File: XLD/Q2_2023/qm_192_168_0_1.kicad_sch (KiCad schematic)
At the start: 113 parts

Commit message: mend
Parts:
- renumbered MX701 to MX1, MX710 to MX10, MX711 to MX11, MX712 to MX12, MX713 to MX13, MX714 to MX14, MX715 to MX15, MX716 to MX16, MX717 to MX17, MX718 to MX18, MX719 to MX19, MX702 to MX2, MX720 to MX20, MX721 to MX21, MX722 to MX22, MX723 to MX23, MX724 to MX24, MX725 to MX25, MX726 to MX26, MX727 to MX27, MX728 to MX28, MX729 to MX29, MX703 to MX3, MX730 to MX30, MX731 to MX31, MX732 to MX32, MX733 to MX33, MX734 to MX34, MX735 to MX35, MX704 to MX4, MX705 to MX5, MX706 to MX6, MX707 to MX7, MX708 to MX8, MX709 to MX9
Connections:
- net ERA_01: now also LO5.
- net ERA_02: now also LO6.
- net ERA_03: now also LO2.
- net ERA_04: now also LO7.
- net ERA_05: now also LO3.
- net ERA_06: now also LO8.
- net ERA_07: now also LO4.
- net ERA_08: now also LO9.
- net LO_01: now also LO10.
- net LO_02: now also LO11.
- net LO_03: now also LO13.
- net LO_04: now also LO14.
- net LO_05: now also LO15.
- net LO_06: now also LO16.
- net LO_08: now also LO12.
- net at Splitter17.: now also Splitter18.; no longer Splitter16.
- net at Splitter18.: no longer Splitter17.
- net at Splitter6.: now also Splitter5.; no longer Splitter8.
- net at Splitter10.: now also Splitter9.; no longer Splitter8.
- net at Splitter22.: no longer Splitter21.
- net at Splitter20.: no longer Splitter21.
- net at Splitter7.: no longer Splitter6.
- net at Splitter5.: no longer Splitter6.
- net at Splitter14.: now also Splitter13.
- net at Splitter13.: now also Splitter12.; no longer Splitter14.
- net at Splitter11.: now also Splitter10.
- net at Splitter12.: no longer Splitter13.
- net at Splitter1.: no longer Splitter2.
- net at Splitter3.: no longer Splitter2.
- net at Splitter4.: now also Splitter3.
- new net: Splitter16., Splitter17.
- new net: Splitter15., Splitter17.
- new net: Splitter6., Splitter8.
- new net: Splitter10., Splitter8.
- new net: Splitter21., Splitter22.
- new net: Splitter20., Splitter21.
- new net: Splitter6., Splitter7.
- new net: Splitter13., Splitter15.
- new net: Splitter1., Splitter2.
- new net: Splitter2., Splitter3.
- now unconnected: Splitter3.
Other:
- moved on the sheet: BT1, BT10, BT11, BT12, BT13, BT14, BT15, BT16, BT2, BT3, BT4, BT5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

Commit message: more updates
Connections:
- net at Splitter17.: now also Splitter18.; no longer Splitter16.
- net at Splitter18.: no longer Splitter17.
- net at Splitter6.: now also Splitter5.; no longer Splitter8.
- net at Splitter10.: now also Splitter9.; no longer Splitter8.
- net at Splitter22.: no longer Splitter21.
- net at Splitter20.: no longer Splitter21.
- net at Splitter7.: no longer Splitter6.
- net at Splitter5.: no longer Splitter6.
- net at Splitter14.: now also Splitter13.
- net at Splitter13.: now also Splitter12.; no longer Splitter14.
- net at Splitter11.: now also Splitter10.
- net at Splitter12.: no longer Splitter13.
- net at Splitter1.: no longer Splitter2.
- net at Splitter3.: no longer Splitter2.
- net at Splitter4.: now also Splitter3.
- new net: Splitter16., Splitter17.
- new net: Splitter15., Splitter17.
- new net: Splitter6., Splitter8.
- new net: Splitter10., Splitter8.
- new net: Splitter21., Splitter22.
- new net: Splitter20., Splitter21.
- new net: Splitter6., Splitter7.
- new net: Splitter13., Splitter15.
- new net: Splitter1., Splitter2.
- new net: Splitter2., Splitter3.
- now unconnected: Splitter3.

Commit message: Improvements to library components, title, date
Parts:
- MX1, MX2, MX3: value SpinQ_IQ -> SpinQ; symbol Quantum Computing:SpinQ_IQ -> Quantum Computing:Mixer IQ SpinQ
- MX10, MX11, MX29, MX30, MX31: value Marki_IQ -> Marki; symbol Quantum Computing:Marki_IQ -> Quantum Computing:Mixer IQ Marki
- MX12: renamed from MX21; value SpinQ_IQ -> SpinQ; symbol Quantum Computing:SpinQ_IQ -> Quantum Computing:Mixer IQ SpinQ
- MX13: renamed from MX16; value Marki_IQ -> Marki; symbol Quantum Computing:Marki_IQ -> Quantum Computing:Mixer IQ Marki
- MX14: renamed from MX17; value Marki_IQ -> Marki; symbol Quantum Computing:Marki_IQ -> Quantum Computing:Mixer IQ Marki
- MX15: renamed from MX22; value SpinQ_IQ -> SpinQ; symbol Quantum Computing:SpinQ_IQ -> Quantum Computing:Mixer IQ SpinQ
- MX16: renamed from MX23; value Marki_IQ -> Marki; symbol Quantum Computing:Marki_IQ -> Quantum Computing:Mixer IQ Marki
- MX17: renamed from MX24; value Marki_IQ -> Marki; symbol Quantum Computing:Marki_IQ -> Quantum Computing:Mixer IQ Marki
- MX18: renamed from MX4; value SpinQ_IQ -> SpinQ; symbol Quantum Computing:SpinQ_IQ -> Quantum Computing:Mixer IQ SpinQ
- MX19: renamed from MX5; value SpinQ_IQ -> SpinQ; symbol Quantum Computing:SpinQ_IQ -> Quantum Computing:Mixer IQ SpinQ
- MX20: renamed from MX27; value Marki_IQ -> Marki; symbol Quantum Computing:Marki_IQ -> Quantum Computing:Mixer IQ Marki
- MX21: renamed from MX6; value SpinQ_IQ -> SpinQ; symbol Quantum Computing:SpinQ_IQ -> Quantum Computing:Mixer IQ SpinQ
- MX22: renamed from MX15; value SpinQ_IQ -> SpinQ; symbol Quantum Computing:SpinQ_IQ -> Quantum Computing:Mixer IQ SpinQ
- MX23: renamed from MX28; value Marki_IQ -> Marki; symbol Quantum Computing:Marki_IQ -> Quantum Computing:Mixer IQ Marki
- MX24: renamed from MX34; value Marki_IQ -> Marki; symbol Quantum Computing:Marki_IQ -> Quantum Computing:Mixer IQ Marki
- MX25: renamed from MX35; value Marki_IQ -> Marki; symbol Quantum Computing:Marki_IQ -> Quantum Computing:Mixer IQ Marki
- MX26: renamed from MX13; value Marki_IQ -> Marki; symbol Quantum Computing:Marki_IQ -> Quantum Computing:Mixer IQ Marki
- MX27: renamed from MX14; value Marki_IQ -> Marki; symbol Quantum Computing:Marki_IQ -> Quantum Computing:Mixer IQ Marki
- MX28: renamed from MX20; value Marki_IQ -> Marki; symbol Quantum Computing:Marki_IQ -> Quantum Computing:Mixer IQ Marki
- MX32: renamed from MX25; value Marki_IQ -> Marki; symbol Quantum Computing:Marki_IQ -> Quantum Computing:Mixer IQ Marki
- MX33: renamed from MX26; value Marki_IQ -> Marki; symbol Quantum Computing:Marki_IQ -> Quantum Computing:Mixer IQ Marki
- MX34: renamed from MX32; value Marki_IQ -> Marki; symbol Quantum Computing:Marki_IQ -> Quantum Computing:Mixer IQ Marki
- MX35: renamed from MX33; value Marki_IQ -> Marki; symbol Quantum Computing:Marki_IQ -> Quantum Computing:Mixer IQ Marki
- MX4: renamed from MX7; value SpinQ_IQ -> SpinQ; symbol Quantum Computing:SpinQ_IQ -> Quantum Computing:Mixer IQ SpinQ
- MX5: renamed from MX8; value SpinQ_IQ -> SpinQ; symbol Quantum Computing:SpinQ_IQ -> Quantum Computing:Mixer IQ SpinQ
- MX6: renamed from MX9; value SpinQ_IQ -> SpinQ; symbol Quantum Computing:SpinQ_IQ -> Quantum Computing:Mixer IQ SpinQ
- MX7: renamed from MX12; value SpinQ_IQ -> SpinQ; symbol Quantum Computing:SpinQ_IQ -> Quantum Computing:Mixer IQ SpinQ
- MX8: renamed from MX18; value SpinQ_IQ -> SpinQ; symbol Quantum Computing:SpinQ_IQ -> Quantum Computing:Mixer IQ SpinQ
- MX9: renamed from MX19; value SpinQ_IQ -> SpinQ; symbol Quantum Computing:SpinQ_IQ -> Quantum Computing:Mixer IQ SpinQ
- Splitter1, Splitter10, Splitter11, Splitter12, Splitter13, Splitter14, Splitter15, Splitter16, Splitter17, Splitter18, Splitter19, Splitter2, Splitter20, Splitter21, Splitter22, Splitter3, Splitter5, Splitter6, Splitter7, Splitter8, Splitter9: symbol Quantum Computing:ZFRSC_183_S+ -> Quantum Computing:Splitter ZFRSC_183_S+
- Splitter4: symbol Quantum Computing:ZFSC-2-10G+ -> Quantum Computing:Splitter ZFSC-2-10G+
- T1: renamed from Ω1; value 50_cap -> Terminator; symbol Quantum Computing:50_cap -> Quantum Computing:Terminator 50ohms
- T10: renamed from Ω2; value 50_cap -> Terminator; symbol Quantum Computing:50_cap -> Quantum Computing:Terminator 50ohms
- T11: renamed from Ω16; value 50_cap -> Terminator; symbol Quantum Computing:50_cap -> Quantum Computing:Terminator 50ohms
- T12: renamed from Ω5; value 50_cap -> Terminator; symbol Quantum Computing:50_cap -> Quantum Computing:Terminator 50ohms
- T13: renamed from Ω8; value 50_cap -> Terminator; symbol Quantum Computing:50_cap -> Quantum Computing:Terminator 50ohms
- T14: renamed from Ω13; value 50_cap -> Terminator; symbol Quantum Computing:50_cap -> Quantum Computing:Terminator 50ohms
- T15: renamed from Ω11; value 50_cap -> Terminator; symbol Quantum Computing:50_cap -> Quantum Computing:Terminator 50ohms
- T16: renamed from Ω14; value 50_cap -> Terminator; symbol Quantum Computing:50_cap -> Quantum Computing:Terminator 50ohms
- T2: renamed from Ω3; value 50_cap -> Terminator; symbol Quantum Computing:50_cap -> Quantum Computing:Terminator 50ohms
- T3: renamed from Ω4; value 50_cap -> Terminator; symbol Quantum Computing:50_cap -> Quantum Computing:Terminator 50ohms
- T4: renamed from Ω6; value 50_cap -> Terminator; symbol Quantum Computing:50_cap -> Quantum Computing:Terminator 50ohms
- T5: renamed from Ω7; value 50_cap -> Terminator; symbol Quantum Computing:50_cap -> Quantum Computing:Terminator 50ohms
- T6: renamed from Ω9; value 50_cap -> Terminator; symbol Quantum Computing:50_cap -> Quantum Computing:Terminator 50ohms
- T7: renamed from Ω10; value 50_cap -> Terminator; symbol Quantum Computing:50_cap -> Quantum Computing:Terminator 50ohms
- T8: renamed from Ω12; value 50_cap -> Terminator; symbol Quantum Computing:50_cap -> Quantum Computing:Terminator 50ohms
- T9: renamed from Ω15; value 50_cap -> Terminator; symbol Quantum Computing:50_cap -> Quantum Computing:Terminator 50ohms
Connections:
- net at Splitter17.: now also Splitter18.; no longer Splitter16.
- net at Splitter18.: no longer Splitter17.
- net at Splitter6.: now also Splitter5.; no longer Splitter8.
- net at Splitter10.: now also Splitter9.; no longer Splitter8.
- net at Splitter22.: no longer Splitter21.
- net at Splitter20.: no longer Splitter21.
- net at Splitter7.: no longer Splitter6.
- net at Splitter5.: no longer Splitter6.
- net at Splitter14.: now also Splitter13.
- net at Splitter13.: now also Splitter12.; no longer Splitter14.
- net at Splitter11.: now also Splitter10.
- net at Splitter12.: no longer Splitter13.
- net at Splitter1.: no longer Splitter2.
- net at Splitter3.: no longer Splitter2.
- net at Splitter4.: now also Splitter3.
- new net: Splitter16., Splitter17.
- new net: Splitter15., Splitter17.
- new net: Splitter6., Splitter8.
- new net: Splitter10., Splitter8.
- new net: Splitter21., Splitter22.
- new net: Splitter20., Splitter21.
- new net: Splitter6., Splitter7.
- new net: Splitter13., Splitter15.
- new net: Splitter1., Splitter2.
- new net: Splitter2., Splitter3.
- now unconnected: Splitter3.
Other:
- company: (none) -> Technology Innovation Institute
- title: (none) -> XLD Setup Q2 2023

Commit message: correct L2-12 LNA gnd, it was fixed. Changed the IQM5q drive line LP to the correct cut frequency.
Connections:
- net at Splitter17.: now also Splitter18.; no longer Splitter16.
- net at Splitter18.: no longer Splitter17.
- net at Splitter6.: now also Splitter5.; no longer Splitter8.
- net at Splitter10.: now also Splitter9.; no longer Splitter8.
- net at Splitter22.: no longer Splitter21.
- net at Splitter20.: no longer Splitter21.
- net at Splitter7.: no longer Splitter6.
- net at Splitter5.: no longer Splitter6.
- net at Splitter14.: now also Splitter13.
- net at Splitter13.: now also Splitter12.; no longer Splitter14.
- net at Splitter11.: now also Splitter10.
- net at Splitter12.: no longer Splitter13.
- net at Splitter1.: no longer Splitter2.
- net at Splitter3.: no longer Splitter2.
- net at Splitter4.: now also Splitter3.
- new net: Splitter16., Splitter17.
- new net: Splitter15., Splitter17.
- new net: Splitter6., Splitter8.
- new net: Splitter10., Splitter8.
- new net: Splitter21., Splitter22.
- new net: Splitter20., Splitter21.
- new net: Splitter6., Splitter7.
- new net: Splitter13., Splitter15.
- new net: Splitter1., Splitter2.
- new net: Splitter2., Splitter3.
- now unconnected: Splitter3.

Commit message: update tii1qb11
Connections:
- net at Splitter17.: now also Splitter18.; no longer Splitter16.
- net at Splitter18.: no longer Splitter17.
- net at Splitter6.: now also Splitter5.; no longer Splitter8.
- net at Splitter10.: now also Splitter9.; no longer Splitter8.
- net at Splitter22.: no longer Splitter21.
- net at Splitter20.: no longer Splitter21.
- net at Splitter7.: no longer Splitter6.
- net at Splitter5.: no longer Splitter6.
- net at Splitter14.: now also Splitter13.
- net at Splitter13.: now also Splitter12.; no longer Splitter14.
- net at Splitter11.: now also Splitter10.
- net at Splitter12.: no longer Splitter13.
- net at Splitter1.: no longer Splitter2.
- net at Splitter3.: no longer Splitter2.
- net at Splitter4.: now also Splitter3.
- new net: Splitter16., Splitter17.
- new net: Splitter15., Splitter17.
- new net: Splitter6., Splitter8.
- new net: Splitter10., Splitter8.
- new net: Splitter21., Splitter22.
- new net: Splitter20., Splitter21.
- new net: Splitter6., Splitter7.
- new net: Splitter13., Splitter15.
- new net: Splitter1., Splitter2.
- new net: Splitter2., Splitter3.
- now unconnected: Splitter3.

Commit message: fix qw5q twpa pump line ip address
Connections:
- net at Splitter17.: now also Splitter18.; no longer Splitter16.
- net at Splitter18.: no longer Splitter17.
- net at Splitter6.: now also Splitter5.; no longer Splitter8.
- net at Splitter10.: now also Splitter9.; no longer Splitter8.
- net at Splitter22.: no longer Splitter21.
- net at Splitter20.: no longer Splitter21.
- net at Splitter7.: no longer Splitter6.
- net at Splitter5.: no longer Splitter6.
- net at Splitter14.: now also Splitter13.
- net at Splitter13.: now also Splitter12.; no longer Splitter14.
- net at Splitter11.: now also Splitter10.
- net at Splitter12.: no longer Splitter13.
- net at Splitter1.: no longer Splitter2.
- net at Splitter3.: no longer Splitter2.
- net at Splitter4.: now also Splitter3.
- new net: Splitter16., Splitter17.
- new net: Splitter15., Splitter17.
- new net: Splitter6., Splitter8.
- new net: Splitter10., Splitter8.
- new net: Splitter21., Splitter22.
- new net: Splitter20., Splitter21.
- new net: Splitter6., Splitter7.
- new net: Splitter13., Splitter15.
- new net: Splitter1., Splitter2.
- new net: Splitter2., Splitter3.
- now unconnected: Splitter3.

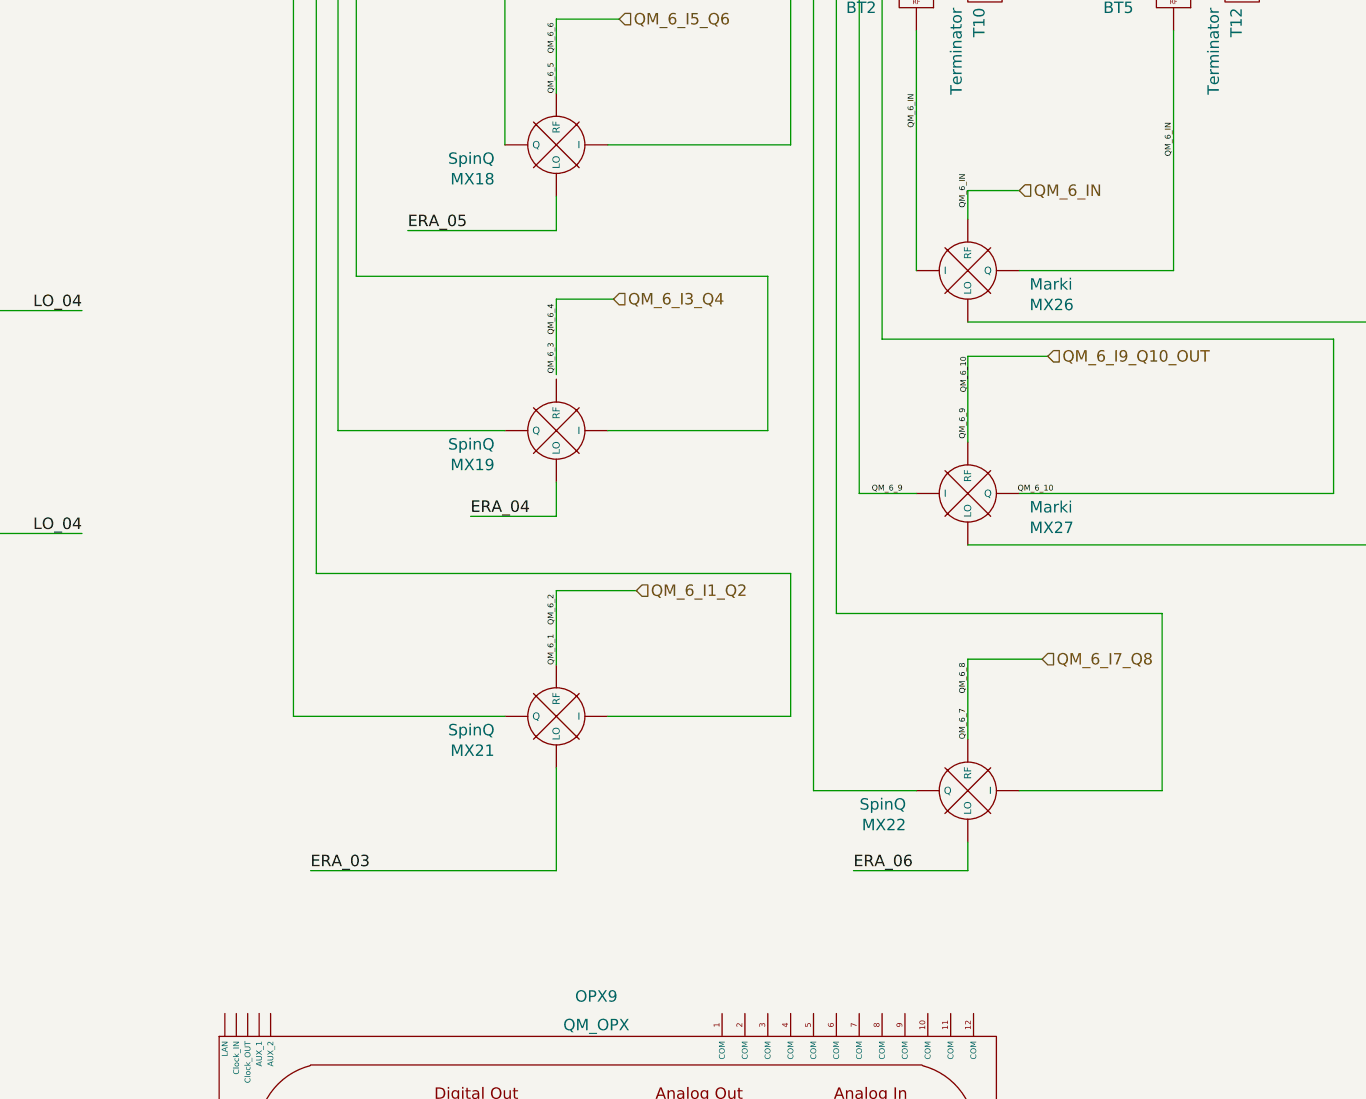
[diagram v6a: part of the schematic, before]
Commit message: disconnect los from line c to use them to pump twpas
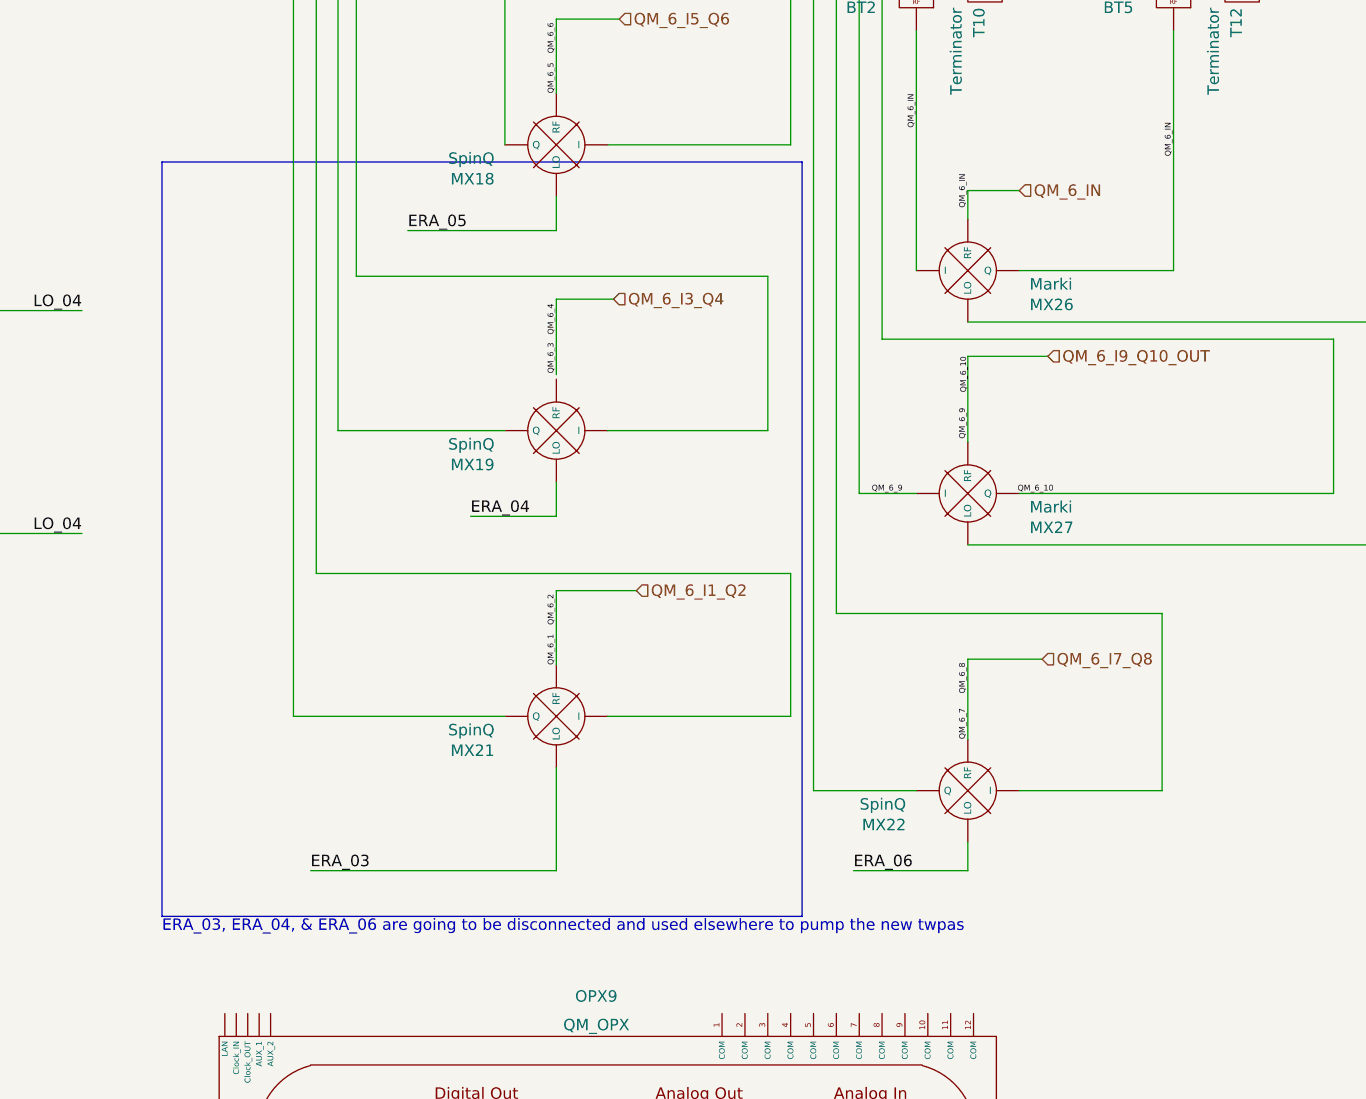
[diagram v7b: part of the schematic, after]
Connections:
- net at Splitter17.: now also Splitter18.; no longer Splitter16.
- net at Splitter18.: no longer Splitter17.
- net at Splitter6.: now also Splitter5.; no longer Splitter8.
- net at Splitter10.: now also Splitter9.; no longer Splitter8.
- net at Splitter22.: no longer Splitter21.
- net at Splitter20.: no longer Splitter21.
- net at Splitter7.: no longer Splitter6.
- net at Splitter5.: no longer Splitter6.
- net at Splitter14.: now also Splitter13.
- net at Splitter13.: now also Splitter12.; no longer Splitter14.
- net at Splitter11.: now also Splitter10.
- net at Splitter12.: no longer Splitter13.
- net at Splitter1.: no longer Splitter2.
- net at Splitter3.: no longer Splitter2.
- net at Splitter4.: now also Splitter3.
- new net: Splitter16., Splitter17.
- new net: Splitter15., Splitter17.
- new net: Splitter6., Splitter8.
- new net: Splitter10., Splitter8.
- new net: Splitter21., Splitter22.
- new net: Splitter20., Splitter21.
- new net: Splitter6., Splitter7.
- new net: Splitter13., Splitter15.
- new net: Splitter1., Splitter2.
- new net: Splitter2., Splitter3.
- now unconnected: Splitter3.
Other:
- note added: "ERA_03, ERA_04, & ERA_06 are going to be disconnected and used elsewhere to pump the new twpas"
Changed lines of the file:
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@@
     (stroke (width 0) (type default))
+  )
+  (rectangle (start 307.34 93.345) (end 378.46 177.165)
+    (stroke (width 0) (type default))
+    (fill (type none))
   )
   (text "192.168.000.208" (at 180.34 384.81 0)
@@
     (effects (font (size 1.27 1.27)) (justify left bottom))
   )
+  (text "ERA_03, ERA_04, & ERA_06 are going to be disconnected and used elsewhere to pump the new twpas"
+    (at 307.34 179.07 0)
+    (effects (font (size 1.27 1.27)) (justify left bottom))
+  )
